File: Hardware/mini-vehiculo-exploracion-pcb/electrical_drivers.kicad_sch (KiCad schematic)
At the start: 13 parts, among them IC1 MAX8891EXK33_V+T, U3 TPS561208DDCR

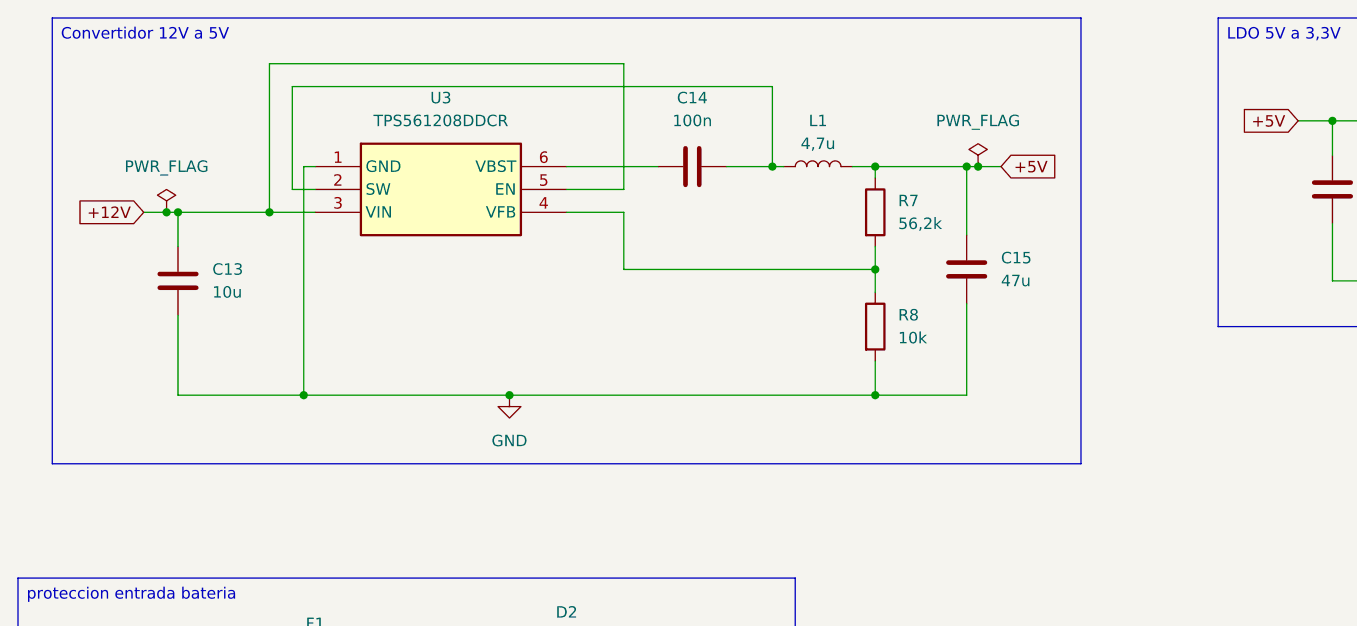
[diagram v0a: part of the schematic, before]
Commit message: adicion de bornera pcb drivers y organizacion de entrada
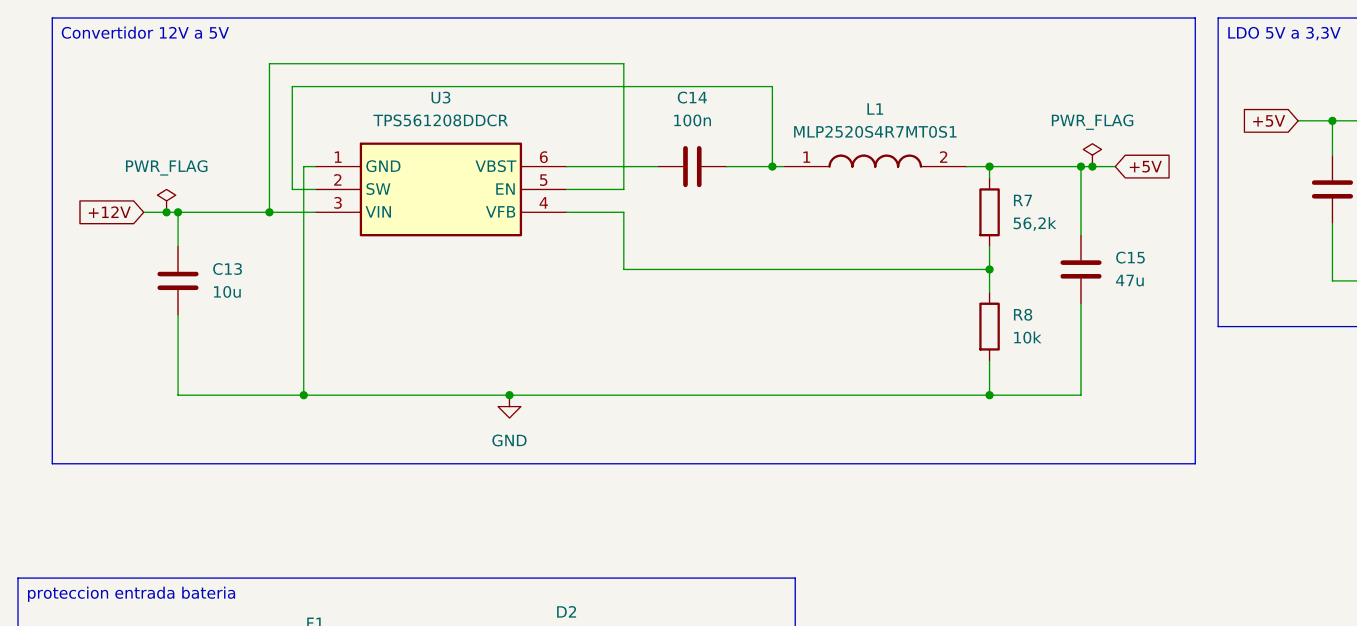
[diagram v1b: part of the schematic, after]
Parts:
- removed L1: 4,7u, symbol Device:L
- added L1: MLP2520S4R7MT0S1, INDC2520X100N, symbol MLP2520S4R7MT0S1:MLP2520S4R7MT0S1
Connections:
- net +5V: now also L1.2
- net at C14.2, U3.2 (SW): now also L1.1
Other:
- moved on the sheet: C15, R7, R8
